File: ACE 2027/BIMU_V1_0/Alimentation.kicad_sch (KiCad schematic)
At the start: 5 parts, among them U101 TLV75801PDRVR

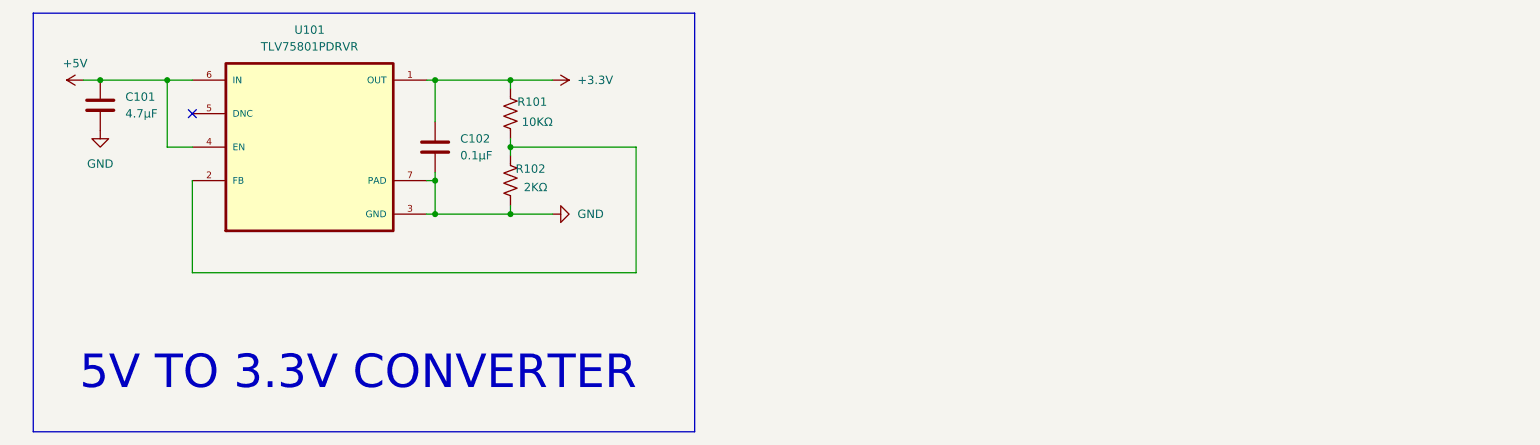
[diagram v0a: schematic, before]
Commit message: Avancement of different part of the schematic
Add and reorganize numerous symbol definitions and annotations in Alimentation.kicad_sch: new TestPoint, LED, R_US/Resistor symbols, BAV99 diode, MountingHole, AP7361C-33E regulator, power/GND symbol instances, and associated symbol variants. Add global CAN_P/CAN_N labels, layout rectangles and text (ESD protection, current rating), and adjust wires/junction coordinates. Also update BIMU_V_1.kicad_pcb, BIMU_V_1.kicad_sch, Capteur.kicad_sch, Controle.kicad_sch and fp-info-cache; add several backup .zip files and a Controle.kicad_sch-bak file.
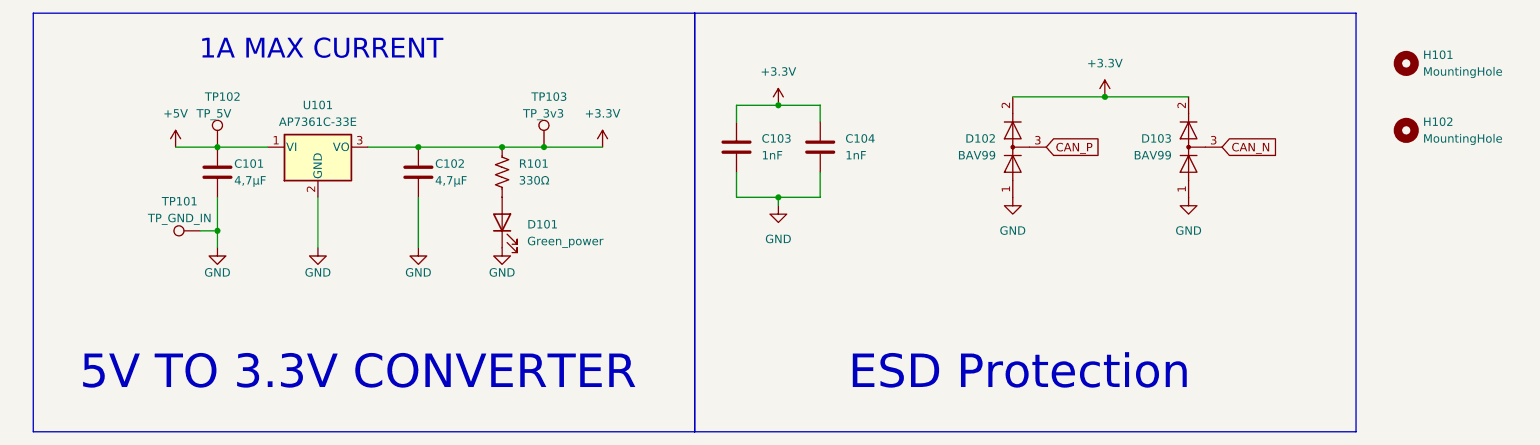
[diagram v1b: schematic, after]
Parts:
- removed R102: 2KΩ, Resistor_SMD:R_0603_1608Metric_Pad0.98x0.95mm_HandSolder, symbol Device:R_US
- removed U101: TLV75801PDRVR, TLV:SON65P200X200X80-7N, symbol TLV75801PDRVR:TLV75801PDRVR
- added C103, C104: 1nF, Capacitor_SMD:C_1812_4532Metric_Pad1.57x3.40mm_HandSolder, symbol Device:C
- added D101: Green_power, Diode_SMD:D_0805_2012Metric, symbol Device:LED
- added D102, D103: BAV99, Package_TO_SOT_SMD:SOT-23, symbol Diode:BAV99
- added H101, H102: MountingHole, MountingHole:MountingHole_3.2mm_M3_ISO14580, symbol Mechanical:MountingHole
- added TP101: TP_GND_IN, Connector_PinHeader_2.54mm:PinHeader_1x01_P2.54mm_Vertical, symbol Connector:TestPoint
- added TP102: TP_5V, Connector_PinHeader_2.54mm:PinHeader_1x01_P2.54mm_Vertical, symbol Connector:TestPoint
- added TP103: TP_3v3, Connector_PinHeader_2.54mm:PinHeader_1x01_P2.54mm_Vertical, symbol Connector:TestPoint
- added U101: AP7361C-33E, Package_TO_SOT_SMD:SOT-223-3_TabPin2, symbol Regulator_Linear:AP7361C-33E
- C101: value 4.7μF -> 4,7µF; footprint Capacitor_SMD:C_0603_1608Metric_Pad1.08x0.95mm_HandSolder -> Capacitor_SMD:C_0805_2012Metric_Pad1.18x1.45mm_HandSolder
- C102: value 0.1μF -> 4,7µF; footprint Capacitor_SMD:C_0603_1608Metric_Pad1.08x0.95mm_HandSolder -> Capacitor_SMD:C_0805_2012Metric_Pad1.18x1.45mm_HandSolder; Digi-Key_PN 1276-6840-1-ND -> (none)
- R101: value 10KΩ -> 330Ω; footprint Resistor_SMD:R_0603_1608Metric_Pad0.98x0.95mm_HandSolder -> Resistor_SMD:R_0805_2012Metric_Pad1.20x1.40mm_HandSolder
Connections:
- net +3.3V: now also R101.1, C103.1, C104.1, D102.2 (A), D103.2 (A), TP103.1, U101.3 (VO); no longer R101.2
- net +5V: now also C101.2, TP102.1, U101.1 (VI); no longer C101.1
- net GND: now also C101.1, C103.2, C104.2, D101.1 (K), D102.1 (K), D103.1 (K), TP101.1, U101.2 (GND); no longer C101.2
- new net: D101.2 (A), R101.2
- new net CAN_N: D103.3 (K)
- new net CAN_P: D102.3 (K)
- no-connect marks 1 -> 0
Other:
- note added: "1A MAX CURRENT"
- note added: "ESD Protection"
